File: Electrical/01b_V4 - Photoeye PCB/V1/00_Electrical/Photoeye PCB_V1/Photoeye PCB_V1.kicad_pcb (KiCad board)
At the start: 2 copper layers, 50 x 20 mm, 13 parts, among them J1 B3B-PH-SM4-TB(LF)(SN), J2 B3B-PH-SM4-TB(LF)(SN), U1 LM293ST, U2 RPR-220

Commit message: fixing the crossed wire for the photo sensor. deleting the old CNC jobs. Re-exporting gerbers and schematics. Re-mill with new files
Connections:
- U2 pad 3: /platterSensor -> +3.3V
- U2 pad 4: +3.3V -> /platterSensor
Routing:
- net +3.3V: track 78.5 -> 82.5 mm
- net /platterSensor: track 26.9 -> 24.6 mm
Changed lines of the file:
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@@
 			(layers "*.Cu" "*.Mask")
 			(remove_unused_layers no)
-			(net 8 "/platterSensor")
+			(net 2 "+3.3V")
 			(pinfunction "E")
 			(pintype "passive")
@@
 			(layers "*.Cu" "*.Mask")
 			(remove_unused_layers no)
-			(net 2 "+3.3V")
+			(net 8 "/platterSensor")
 			(pinfunction "C")
 			(pintype "passive")
@@
 	)
 	(segment
+		(start 130.7 97.8375)
+		(end 130.7 100.2)
+		(width 0.5)
+		(layer "F.Cu")
+		(net 2)
+	)
+	(segment
 		(start 148.5 89.9)
 		(end 152.75 89.9)
@@
 	)
 	(segment
+		(start 146.725 96.725)
+		(end 147 97)
+		(width 0.5)
+		(layer "F.Cu")
+		(net 2)
+	)
+	(segment
+		(start 148.5 89.9)
+		(end 144.675 89.9)
+		(width 0.5)
+		(layer "F.Cu")
+		(net 2)
+	)
+	(segment
+		(start 126.5 95.6375)
+		(end 126.5 95.5)
+		(width 0.5)
+		(layer "F.Cu")
+		(net 2)
+	)
+	(segment
 		(start 128.5 95.6375)
 		(end 130.7 97.8375)
@@
 	)
 	(segment
-		(start 146.725 96.725)
-		(end 147 97)
-		(width 0.5)
-		(layer "F.Cu")
-		(net 2)
-	)
-	(segment
-		(start 148.5 89.9)
-		(end 144.675 89.9)
+		(start 135 97.8375)
+		(end 135.2 97.6375)
 		(width 0.5)
 		(layer "F.Cu")
@@
 	(segment
 		(start 126.5 95.6375)
-		(end 126.5 95.5)
+		(end 128.5 95.6375)
 		(width 0.5)
 		(layer "F.Cu")
@@
 	)
 	(segment
-		(start 130.7 97.8375)
-		(end 132.5 97.8375)
+		(start 135 97.8375)
+		(end 135 98.1375)
 		(width 0.5)
 		(layer "F.Cu")
@@
 	)
 	(segment
+		(start 131.1375 100.6375)
+		(end 132.5 100.6375)
+		(width 0.5)
+		(layer "F.Cu")
+		(net 2)
+	)
+	(segment
 		(start 136 90.5)
 		(end 138 88.5)
@@
 	)
 	(segment
+		(start 135 97.8375)
+		(end 134.8375 97.8375)
+		(width 0.5)
+		(layer "F.Cu")
+		(net 2)
+	)
+	(segment
 		(start 146.190001 102.309999)
 		(end 134.172499 102.309999)
@@
 	)
 	(segment
-		(start 126.5 95.6375)
-		(end 128.5 95.6375)
-		(width 0.5)
-		(layer "F.Cu")
-		(net 2)
-	)
-	(segment
 		(start 127 90.5)
 		(end 136 90.5)
@@
 	)
 	(segment
-		(start 132.5 100.6375)
-		(end 132.5 99)
-		(width 0.5)
-		(layer "F.Cu")
-		(net 2)
-	)
-	(segment
-		(start 132.5 99)
-		(end 132.5 97.8375)
-		(width 0.5)
-		(layer "F.Cu")
-		(net 2)
-	)
-	(segment
 		(start 138 88.5)
 		(end 142.5 88.5)
@@
 	)
 	(segment
+		(start 130.7 100.2)
+		(end 131.1375 100.6375)
+		(width 0.5)
+		(layer "F.Cu")
+		(net 2)
+	)
+	(segment
 		(start 146.725 95.6375)
 		(end 144.213 95.6375)
@@
 		(start 144.2875 90.2875)
 		(end 144.2875 91.1375)
+		(width 0.5)
+		(layer "F.Cu")
+		(net 2)
+	)
+	(segment
+		(start 135 98.1375)
+		(end 132.5 100.6375)
 		(width 0.5)
 		(layer "F.Cu")
@@
 	)
 	(segment
-		(start 135 97.8375)
-		(end 135.2 97.6375)
-		(width 0.5)
-		(layer "F.Cu")
-		(net 8)
-	)
-	(segment
 		(start 129 91.5)
 		(end 130 91.5)
@@
 	)
 	(segment
-		(start 134.8375 97.8375)
-		(end 132.6375 95.6375)
+		(start 131.1375 95.6375)
+		(end 132.5 97)
+		(width 0.5)
+		(layer "F.Cu")
+		(net 8)
+	)
+	(segment
+		(start 131 95.6375)
+		(end 131.1375 95.6375)
 		(width 0.5)
 		(layer "F.Cu")
@@
 		(start 128.3625 93)
 		(end 127.5 93)
-		(width 0.5)
-		(layer "F.Cu")
-		(net 8)
-	)
-	(segment
-		(start 135 97.8375)
-		(end 134.8375 97.8375)
 		(width 0.5)
 		(layer "F.Cu")
@@
 	)
 	(segment
-		(start 132.6375 95.6375)
-		(end 131 95.6375)
-		(width 0.5)
-		(layer "F.Cu")
+		(start 132.5 97.8375)
+		(end 132.5 97)
+		(width 0.5)
+		(layer "F.Cu")

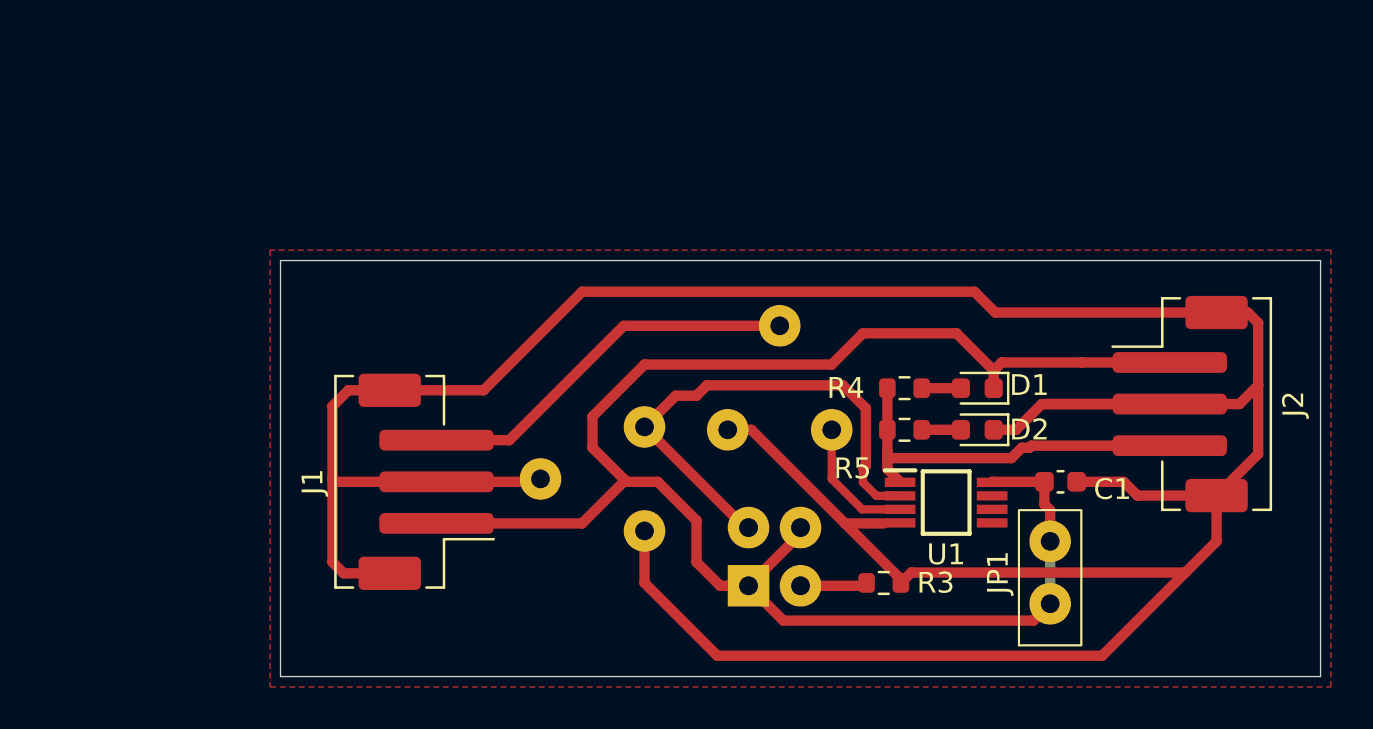
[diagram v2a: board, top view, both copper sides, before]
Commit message: updates to schematic to document outside components. Plans for additional electrical features requiring desiging a few more PCBs
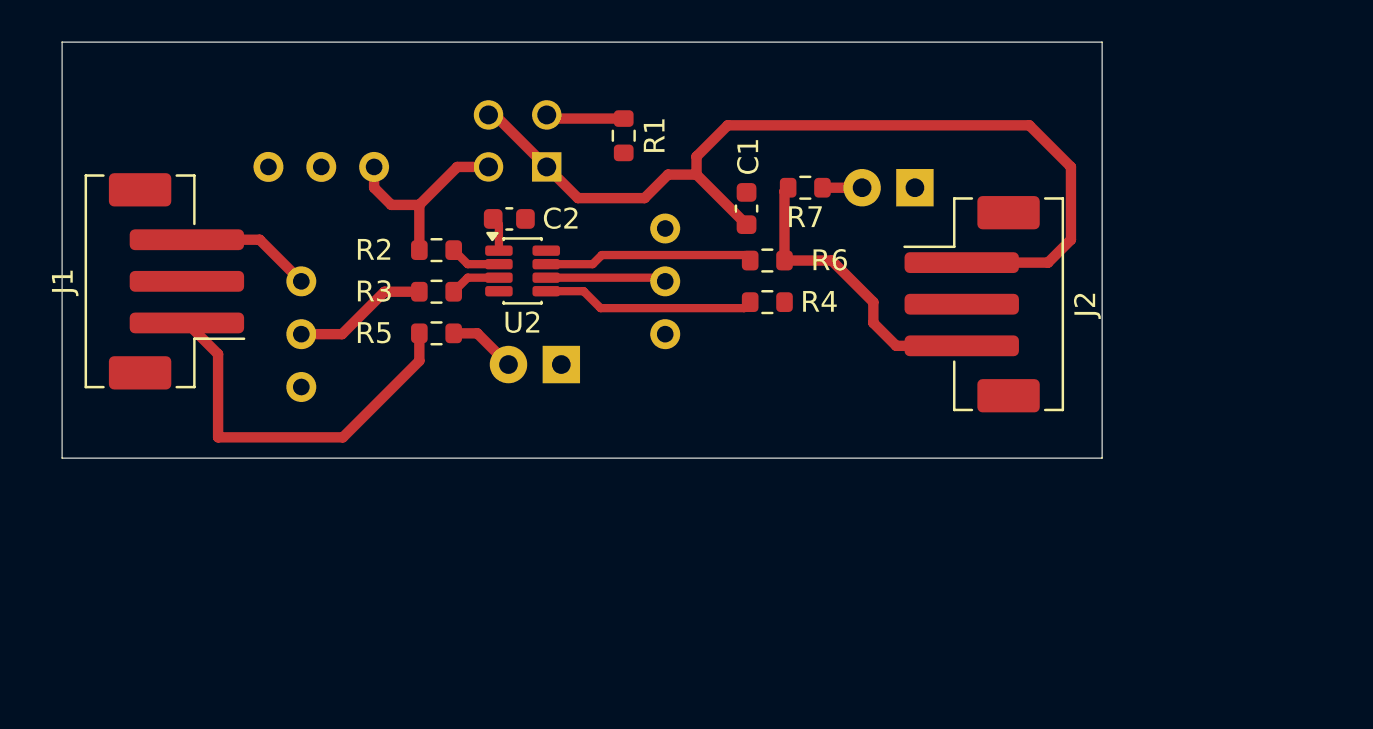
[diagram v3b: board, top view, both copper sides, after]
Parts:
- removed JP1: Jumper_2_Bridged, photoeye_pcb:3mm jumper
- added C2: cap, Capacitor_SMD:C_0603_1608Metric, F.Cu at (121.0, 83.0)
- added R6: 1kohm_0603, Resistor_SMD:R_0603_1608Metric, F.Cu at (133.4, 85.0)
- added R7: 300ohm_0603, Resistor_SMD:R_0603_1608Metric, F.Cu at (135.2, 81.5)
- added RV1: 100kohm pot, Potentiometer_THT:Potentiometer_Bourns_3296W_Vertical, B.Cu at (114.5, 80.5)
- added RV2: R_Potentiometer_US, Potentiometer_THT:Potentiometer_Bourns_3296W_Vertical, B.Cu at (111.0, 86.0)
- added RV3: R_Potentiometer_US, Potentiometer_THT:Potentiometer_Bourns_3296W_Vertical, B.Cu at (128.5, 88.5)
- D1: value RED_0603 -> YELLOW_3mm_LED; footprint LED_SMD:LED_0603_1608Metric -> LED_THT:LED_D3.0mm_Clear; moved to B.Cu
- D2: value GREEN_0603 -> GREEN_3mm_TH; footprint LED_SMD:LED_0603_1608Metric -> LED_THT:LED_D3.0mm; moved to B.Cu
- R1: value 10k_TH_pot -> 100ohm_0603; footprint photoeye_pcb:Potentiometer_TH -> Resistor_SMD:R_0603_1608Metric; moved to F.Cu
- R2: value 100k_TH_Pot -> 1kohm_0603; footprint photoeye_pcb:Potentiometer_TH -> Resistor_SMD:R_0603_1608Metric; moved to F.Cu
- R3: value 100ohm_0603 -> 1kohm_0603
- R5: value 1kohm_0603 -> ohm_0603
- U1: value LM293ST -> RPR-220; footprint photoeye_pcb:LM293ST -> photoeye_pcb:RPR220; moved to B.Cu
- U2: value RPR-220 -> LM358B; footprint photoeye_pcb:RPR220 -> Package_TO_SOT_SMD:SOT-23-8; moved to F.Cu
- moved R3 25.7 mm to (117.5, 86.5)
- moved U1 25.1 mm to (122.8, 80.5), turned to 180 degrees
- moved R5 23.0 mm to (117.5, 88.5), turned to 0 degrees
- moved D1 20.0 mm to (123.5, 90.0)
- moved C1 20.0 mm to (132.4, 82.5), turned to 90 degrees
- moved U2 18.6 mm to (121.6, 85.5), turned to 0 degrees
- moved R1 17.3 mm to (126.5, 79.0)
- moved J1 15.4 mm to (105.0, 86.0)
- moved R2 13.1 mm to (117.5, 84.5)
- moved D2 12.0 mm to (140.5, 81.5)
- moved J2 11.1 mm to (143.2, 87.1)
- moved R4 7.79 mm to (133.4, 87.0), turned to 0 degrees
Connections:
- C1 pad 1: GND -> +3.3V
- C1 pad 2: +3.3V -> GND
- D1 pad 1: +3.3V -> GND
- R1 pad 1: Net-(U1-IN1+) -> GND
- R1 pad 2: Net-(J1-Pin_3) -> Net-(U1-K)
- R2 pad 1: /platterSensor -> Net-(U2A--)
- R2 pad 2: GND -> /platterSensor
- R3 pad 1: GND -> Net-(U2A-+)
- R3 pad 2: Net-(U2-K) -> Net-(R3-Pad2)
- R4 pad 1: Net-(D1-A) -> Net-(U2B-+)
- R4 pad 2: /outputState -> Net-(C2-Pad2)
- R5 pad 1: Net-(D2-A) -> +3.3V
- R5 pad 2: /outputState -> Net-(D1-A)
- U1 pad 1: /outputState -> +3.3V
- U1 pad 2: /platterSensor -> Net-(U1-K)
- U1 pad 3: Net-(U1-IN1+) -> +3.3V
- U1 pad 4: GND -> /platterSensor
- U2 pad 1: +3.3V -> Net-(C2-Pad2)
- U2 pad 2: Net-(U2-K) -> Net-(U2A--)
- U2 pad 3: +3.3V -> Net-(U2A-+)
- U2 pad 4: /platterSensor -> GND
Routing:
- net GND: track 166.9 -> 0.00 mm
- net +3.3V: track 82.3 -> 63.7 mm
- net /platterSensor: track 24.6 -> 9.77 mm
- net Net-(J1-Pin_3): track 18.8 -> 6.33 mm
- net Net-(U2B-+): track 0.00 -> 10.3 mm
- net Net-(R6-Pad2): track 0.00 -> 10.1 mm
- net Net-(R3-Pad2): track 0.00 -> 6.52 mm
- net Net-(U1-IN1+): track 6.26 -> 0.00 mm
- net Net-(U2B--): track 0.00 -> 5.79 mm
- net /outputState: track 18.6 -> 14.4 mm
- net Net-(U1-K): track 0.00 -> 3.77 mm
- net Net-(U2-K): track 3.23 -> 0.00 mm
- net Net-(U2A--): track 0.00 -> 2.45 mm
- net Net-(U2A-+): track 0.00 -> 2.45 mm
- net Net-(C2-Pad2): track 0.00 -> 1.64 mm
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- removed copper zone on F.Cu, net GND
